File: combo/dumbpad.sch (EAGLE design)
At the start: 48 parts

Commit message: fixing bad merge
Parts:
- removed GND2, GND3, GND4, GND6, GND7: GND, supply1:GND
- removed SUPPLY2: VCC, SparkFun-PowerSymbols:VCC
- D1, D10, D11, D12, D13, D14, D15, D16, D2, D20, D3, D4, D5, D6, D7, D8, D9: value DIODEDO-1N4148 -> (none)
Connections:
- removed net ROW3_A: D17.A
- net GND: no longer D20.C, GND2.GND, GND3.GND, GND4.GND, GND6.GND, GND7.GND
- net N$10: no longer D20.A, R3.1
- net N$15: no longer R2.1
- net N$5: no longer D18.A
- net VCC: no longer SUPPLY2.VCC
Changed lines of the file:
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@@
-</segment>
-<segment>
-<pinref part="D18" gate="D1" pin="C"/>
-<wire x1="160.02" y1="134.62" x2="160.02" y2="132.08" width="0.1524" layer="91"/>
-<wire x1="160.02" y1="132.08" x2="165.1" y2="132.08" width="0.1524" layer="91"/>
-<pinref part="GND2" gate="1" pin="GND"/>
-<wire x1="165.1" y1="132.08" x2="165.1" y2="129.54" width="0.1524" layer="91"/>
-<wire x1="165.1" y1="132.08" x2="170.18" y2="132.08" width="0.1524" layer="91"/>
-<junction x="165.1" y="132.08"/>
-<pinref part="D19" gate="D1" pin="C"/>
-<wire x1="170.18" y1="132.08" x2="170.18" y2="134.62" width="0.1524" layer="91"/>
-<wire x1="170.18" y1="132.08" x2="180.34" y2="132.08" width="0.1524" layer="91"/>
-<junction x="170.18" y="132.08"/>
-<pinref part="D20" gate="D1" pin="C"/>
-<wire x1="180.34" y1="132.08" x2="180.34" y2="134.62" width="0.1524" layer="91"/>
 </segment>
 <segment>
@@
 </segment>
 </net>
-<net name="N$5" class="0">
-<segment>
-<pinref part="D18" gate="D1" pin="A"/>
-<pinref part="R1" gate="G$1" pin="1"/>
-<wire x1="160.02" y1="142.24" x2="160.02" y2="147.32" width="0.1524" layer="91"/>
-</segment>
-</net>
-<net name="N$15" class="0">
-<segment>
-<pinref part="R2" gate="G$1" pin="1"/>
-<pinref part="D19" gate="D1" pin="A"/>
-<wire x1="170.18" y1="147.32" x2="170.18" y2="142.24" width="0.1524" layer="91"/>
-</segment>
-</net>
-<net name="LED0" class="0">
-<segment>
-<pinref part="R1" gate="G$1" pin="2"/>
-<wire x1="160.02" y1="157.48" x2="160.02" y2="160.02" width="0.1524" layer="91"/>
-<label x="160.02" y="160.02" size="1.778" layer="95"/>
-</segment>
-<segment>
-<pinref part="B1" gate="G$1" pin="12(MISO)"/>
-<wire x1="294.64" y1="129.54" x2="302.26" y2="129.54" width="0.1524" layer="91"/>
-<label x="302.26" y="129.54" size="1.778" layer="95"/>
-</segment>
-</net>
-<net name="LED1" class="0">
-<segment>
-<pinref part="R2" gate="G$1" pin="2"/>
-<wire x1="170.18" y1="157.48" x2="170.18" y2="160.02" width="0.1524" layer="91"/>
-<label x="170.18" y="160.02" size="1.778" layer="95"/>
-</segment>
-<segment>
-<pinref part="B1" gate="G$1" pin="13(SCK)"/>
-<wire x1="294.64" y1="132.08" x2="302.26" y2="132.08" width="0.1524" layer="91"/>
-<label x="302.26" y="132.08" size="1.778" layer="95"/>
-</segment>
-</net>
-<net name="S17_E" class="0">
-<segment>
-<pinref part="JP1" gate="G$1" pin="3"/>
-<wire x1="228.6" y1="124.46" x2="228.6" y2="121.92" width="0.1524" layer="91"/>
-<wire x1="228.6" y1="121.92" x2="233.68" y2="121.92" width="0.1524" layer="91"/>
-<pinref part="RE1" gate="G$2" pin="2"/>
-<wire x1="233.68" y1="121.92" x2="241.3" y2="121.92" width="0.1524" layer="91"/>
-<wire x1="241.3" y1="121.92" x2="241.3" y2="129.54" width="0.1524" layer="91"/>
-<pinref part="JP2" gate="G$1" pin="1"/>
-<wire x1="233.68" y1="124.46" x2="233.68" y2="121.92" width="0.1524" layer="91"/>
-<junction x="233.68" y="121.92"/>
-<label x="228.6" y="119.38" size="1.778" layer="95"/>
-</segment>
-</net>
-<net name="S17_D" class="0">
-<segment>
-<pinref part="RE1" gate="G$2" pin="1"/>
-<wire x1="251.46" y1="129.54" x2="254" y2="129.54" width="0.1524" layer="91"/>
-<wire x1="254" y1="129.54" x2="254" y2="137.16" width="0.1524" layer="91"/>
-<wire x1="254" y1="137.16" x2="233.68" y2="137.16" width="0.1524" layer="91"/>
-<pinref part="JP1" gate="G$1" pin="1"/>
-<wire x1="233.68" y1="137.16" x2="228.6" y2="137.16" width="0.1524" layer="91"/>
-<wire x1="228.6" y1="134.62" x2="228.6" y2="137.16" width="0.1524" layer="91"/>
-<pinref part="JP2" gate="G$1" pin="3"/>
-<wire x1="233.68" y1="134.62" x2="233.68" y2="137.16" width="0.1524" layer="91"/>
-<junction x="233.68" y="137.16"/>
-<label x="241.3" y="137.16" size="1.778" layer="95"/>
-</segment>
-</net>
-<net name="ROW3_A" class="0">
-<segment>
-<pinref part="JP1" gate="G$1" pin="2"/>
-<pinref part="D17" gate="G$1" pin="A"/>
-<wire x1="218.44" y1="129.54" x2="223.52" y2="129.54" width="0.1524" layer="91"/>
-</segment>
-</net>
-<net name="LED2" class="0">
-<segment>
-<pinref part="B1" gate="G$1" pin="*10"/>
-<wire x1="294.64" y1="124.46" x2="302.26" y2="124.46" width="0.1524" layer="91"/>
-<label x="302.26" y="124.46" size="1.778" layer="95"/>
-</segment>
-<segment>
-<pinref part="R3" gate="G$1" pin="2"/>
-<wire x1="180.34" y1="157.48" x2="180.34" y2="160.02" width="0.1524" layer="91"/>
-<label x="180.34" y="160.02" size="1.778" layer="95"/>
-</segment>
-</net>
-<net name="N$10" class="0">
-<segment>
-<pinref part="D20" gate="D1" pin="A"/>
-<pinref part="R3" gate="G$1" pin="1"/>
-<wire x1="180.34" y1="142.24" x2="180.34" y2="147.32" width="0.1524" layer="91"/>
-</segment>
-</net>
 </nets>
 </sheet>
 </sheets>
-<errors>
-</errors>
 </schematic>
 </drawing>

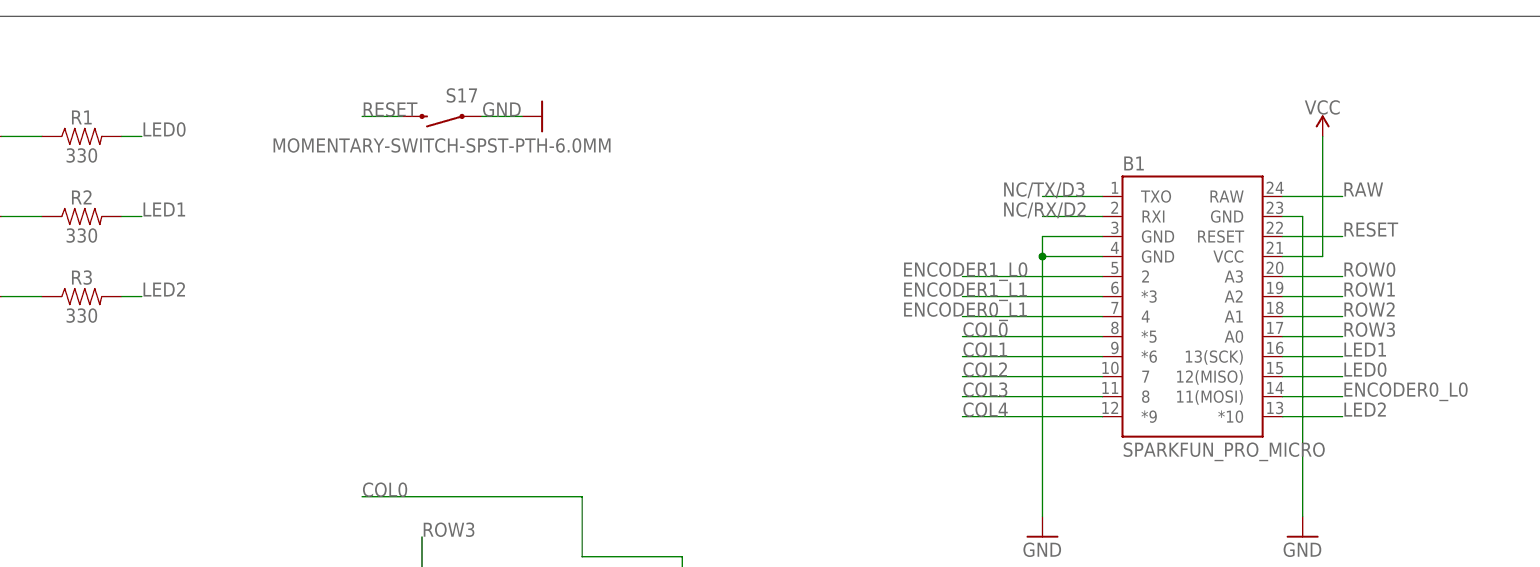
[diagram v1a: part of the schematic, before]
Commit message: fixing naming issue in combo
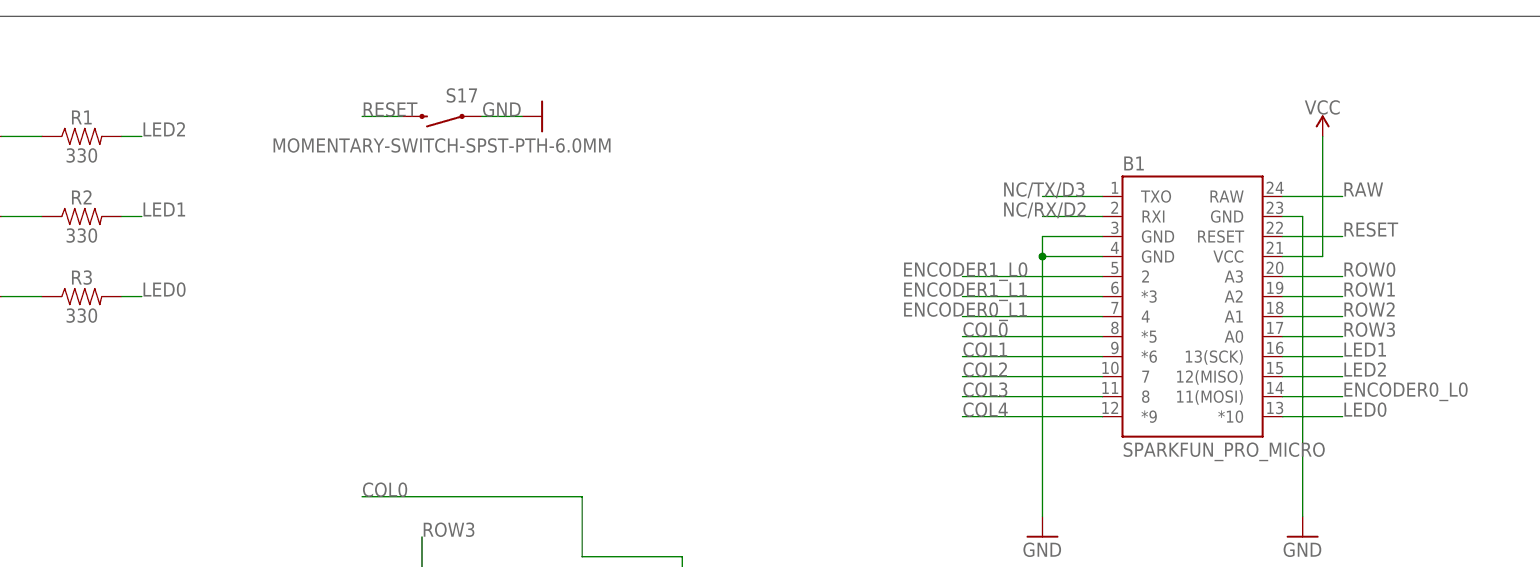
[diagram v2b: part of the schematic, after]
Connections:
- net LED0: now also B1.*10, R3.2; no longer B1.12(MISO), R1.2
- net LED2: now also B1.12(MISO), R1.2; no longer B1.*10, R3.2
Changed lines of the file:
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@@
 <net name="LED0" class="0">
 <segment>
-<pinref part="R1" gate="G$1" pin="2"/>
-<wire x1="160.02" y1="177.8" x2="162.56" y2="177.8" width="0.1524" layer="91" grouprefs="LEDS_RESISTORS"/>
-<label x="162.56" y="177.8" size="1.778" layer="95" grouprefs="LEDS_RESISTORS"/>
+<pinref part="B1" gate="G$1" pin="*10"/>
+<wire x1="307.34" y1="142.24" x2="314.96" y2="142.24" width="0.1524" layer="91" grouprefs="PRO_MICRO"/>
+<label x="314.96" y="142.24" size="1.778" layer="95" grouprefs="PRO_MICRO"/>
 </segment>
 <segment>
-<pinref part="B1" gate="G$1" pin="12(MISO)"/>
-<wire x1="307.34" y1="147.32" x2="314.96" y2="147.32" width="0.1524" layer="91" grouprefs="PRO_MICRO"/>
-<label x="314.96" y="147.32" size="1.778" layer="95" grouprefs="PRO_MICRO"/>
+<pinref part="R3" gate="G$1" pin="2"/>
+<wire x1="160.02" y1="157.48" x2="162.56" y2="157.48" width="0.1524" layer="91" grouprefs="LEDS_RESISTORS"/>
+<label x="162.56" y="157.48" size="1.778" layer="95" grouprefs="LEDS_RESISTORS"/>
 </segment>
 </net>
@@
 <net name="LED2" class="0">
 <segment>
-<pinref part="B1" gate="G$1" pin="*10"/>
-<wire x1="307.34" y1="142.24" x2="314.96" y2="142.24" width="0.1524" layer="91" grouprefs="PRO_MICRO"/>
-<label x="314.96" y="142.24" size="1.778" layer="95" grouprefs="PRO_MICRO"/>
+<pinref part="B1" gate="G$1" pin="12(MISO)"/>
+<wire x1="307.34" y1="147.32" x2="314.96" y2="147.32" width="0.1524" layer="91" grouprefs="PRO_MICRO"/>
+<label x="314.96" y="147.32" size="1.778" layer="95" grouprefs="PRO_MICRO"/>
 </segment>
 <segment>
-<pinref part="R3" gate="G$1" pin="2"/>
-<wire x1="160.02" y1="157.48" x2="162.56" y2="157.48" width="0.1524" layer="91" grouprefs="LEDS_RESISTORS"/>
-<label x="162.56" y="157.48" size="1.778" layer="95" grouprefs="LEDS_RESISTORS"/>
+<pinref part="R1" gate="G$1" pin="2"/>
+<wire x1="160.02" y1="177.8" x2="162.56" y2="177.8" width="0.1524" layer="91" grouprefs="LEDS_RESISTORS"/>
+<label x="162.56" y="177.8" size="1.778" layer="95" grouprefs="LEDS_RESISTORS"/>
 </segment>
 </net>

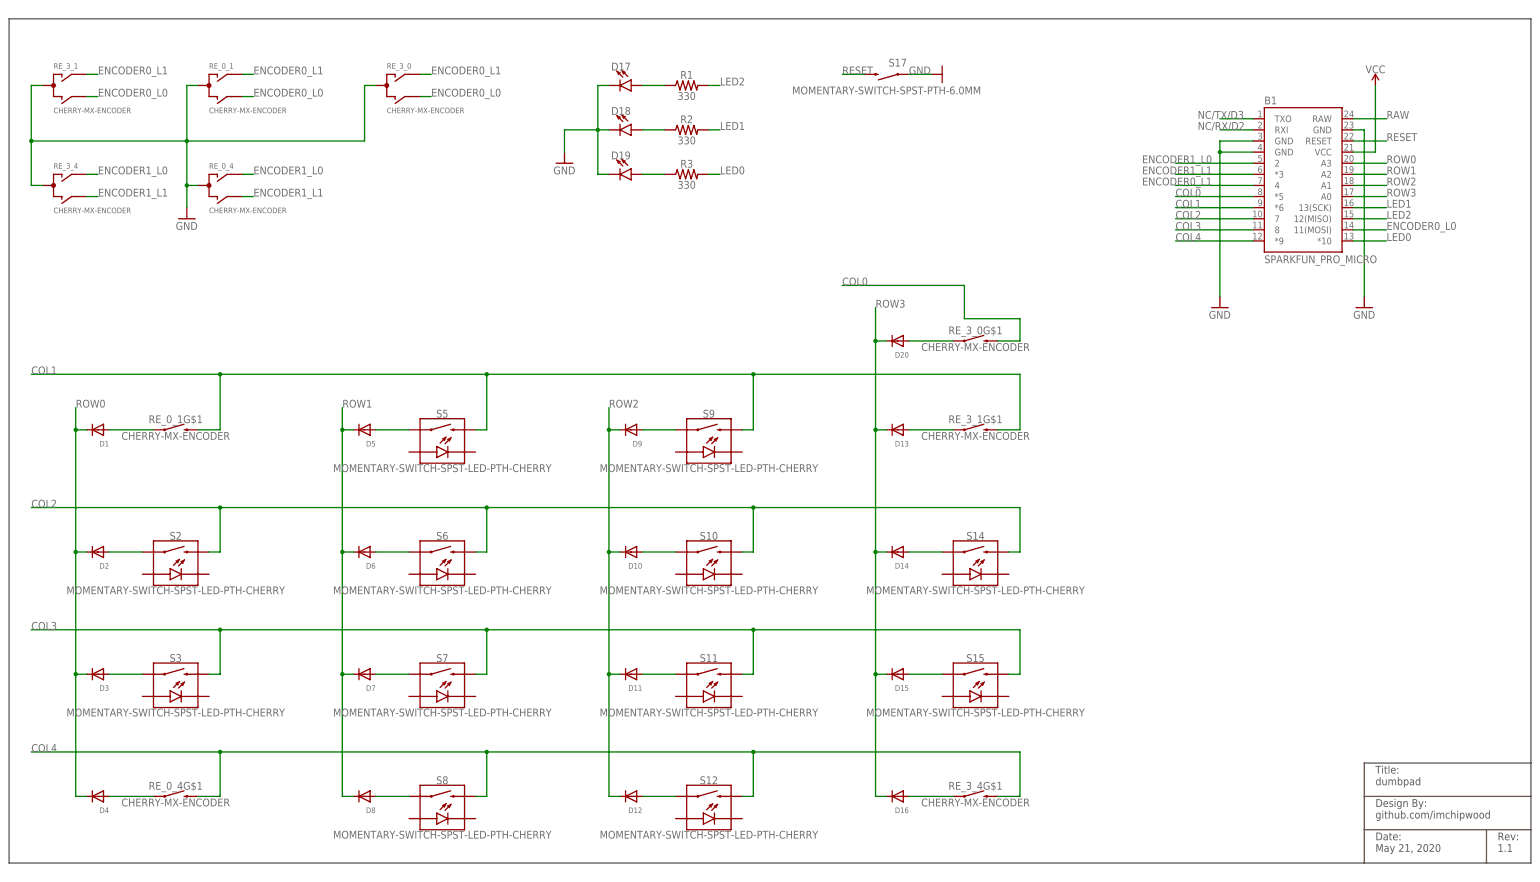
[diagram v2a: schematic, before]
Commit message: fixed encoder pin naming mismatch, updated screenshot
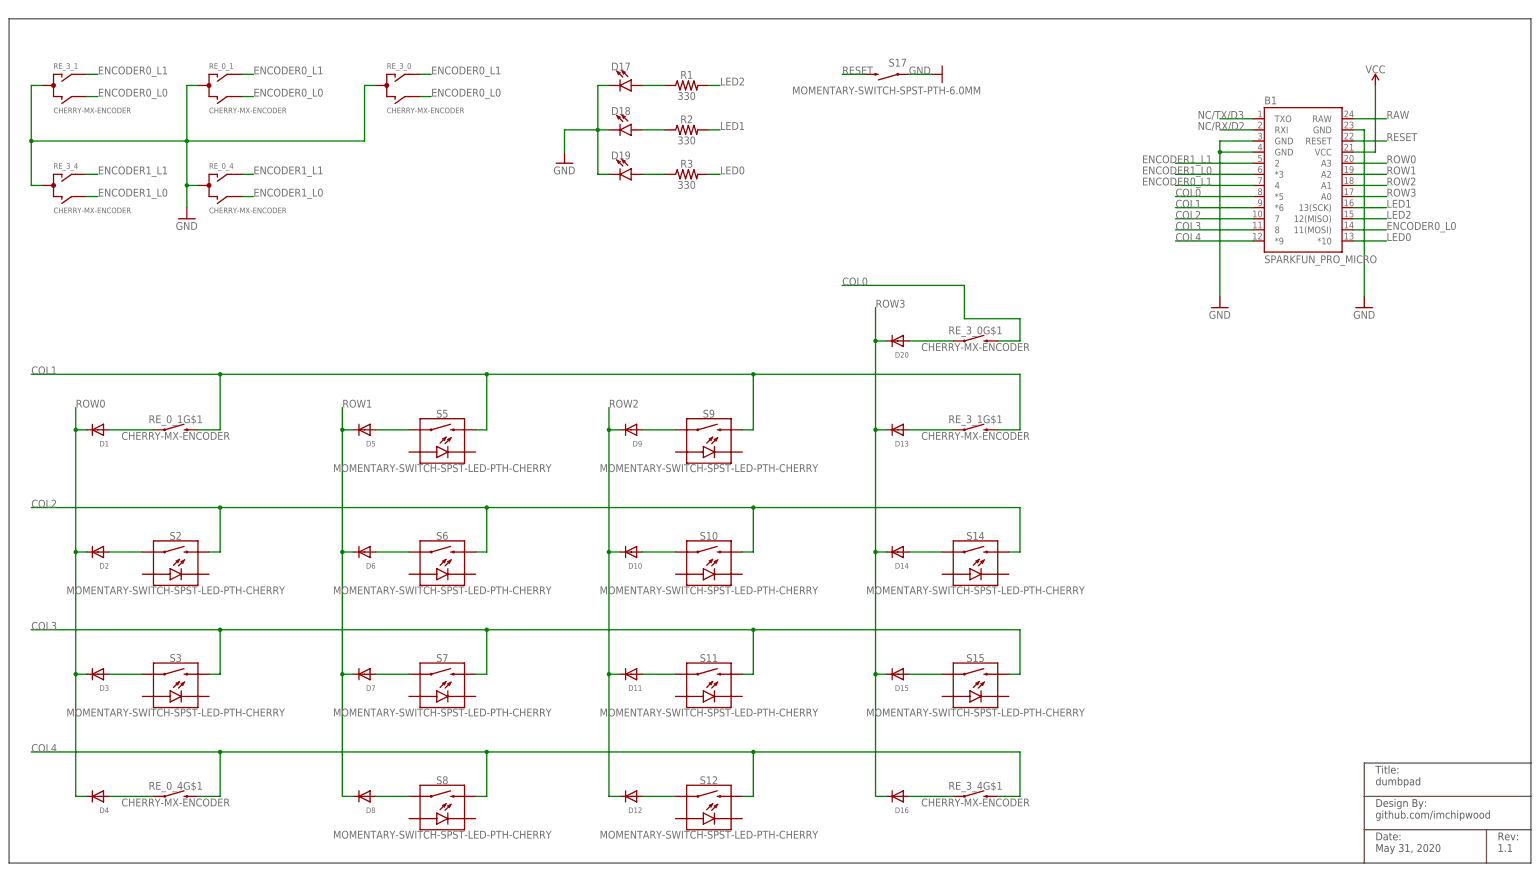
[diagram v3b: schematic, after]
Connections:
- net ENCODER1_L0: now also B1.*3, RE_0_4G$2.B, RE_3_4G$2.B; no longer B1.2, RE_0_4G$2.A, RE_3_4G$2.A
- net ENCODER1_L1: now also B1.2, RE_0_4G$2.A, RE_3_4G$2.A; no longer B1.*3, RE_0_4G$2.B, RE_3_4G$2.B
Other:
- note added: "Date: May 31, 2020"
- note removed: "Date: May 21, 2020"
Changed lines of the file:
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@@
 1.1</text>
 <text x="312.42" y="2.54" size="1.778" layer="97">Date:
-May 21, 2020</text>
+May 31, 2020</text>
 <text x="312.42" y="10.16" size="1.778" layer="97">Design By:
 github.com/imchipwood</text>
@@
 </segment>
 </net>
-<net name="ENCODER1_L0" class="0">
+<net name="ENCODER1_L1" class="0">
 <segment>
 <wire x1="17.78" y1="157.48" x2="20.32" y2="157.48" width="0.1524" layer="91" grouprefs="ENCODER_PINS"/>
@@
 </segment>
 </net>
-<net name="ENCODER1_L1" class="0">
+<net name="ENCODER1_L0" class="0">
 <segment>
 <wire x1="17.78" y1="152.4" x2="20.32" y2="152.4" width="0.1524" layer="91" grouprefs="ENCODER_PINS"/>
